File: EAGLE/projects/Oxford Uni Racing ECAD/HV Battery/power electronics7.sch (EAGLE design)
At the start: 57 parts, among them IC1 4043D, IC2 SE555D, IC6 4011D, K1 T9AS1D12-48=T9A, K2 T9AS5D12-12=T9A, K3 T9AS1D12-48=T9A, K4 T9AS1D12-48=T9A, K5 T9AS1D12-48=T9A, Q1 BSS138, Q2 BSS138, Q3 BSS138

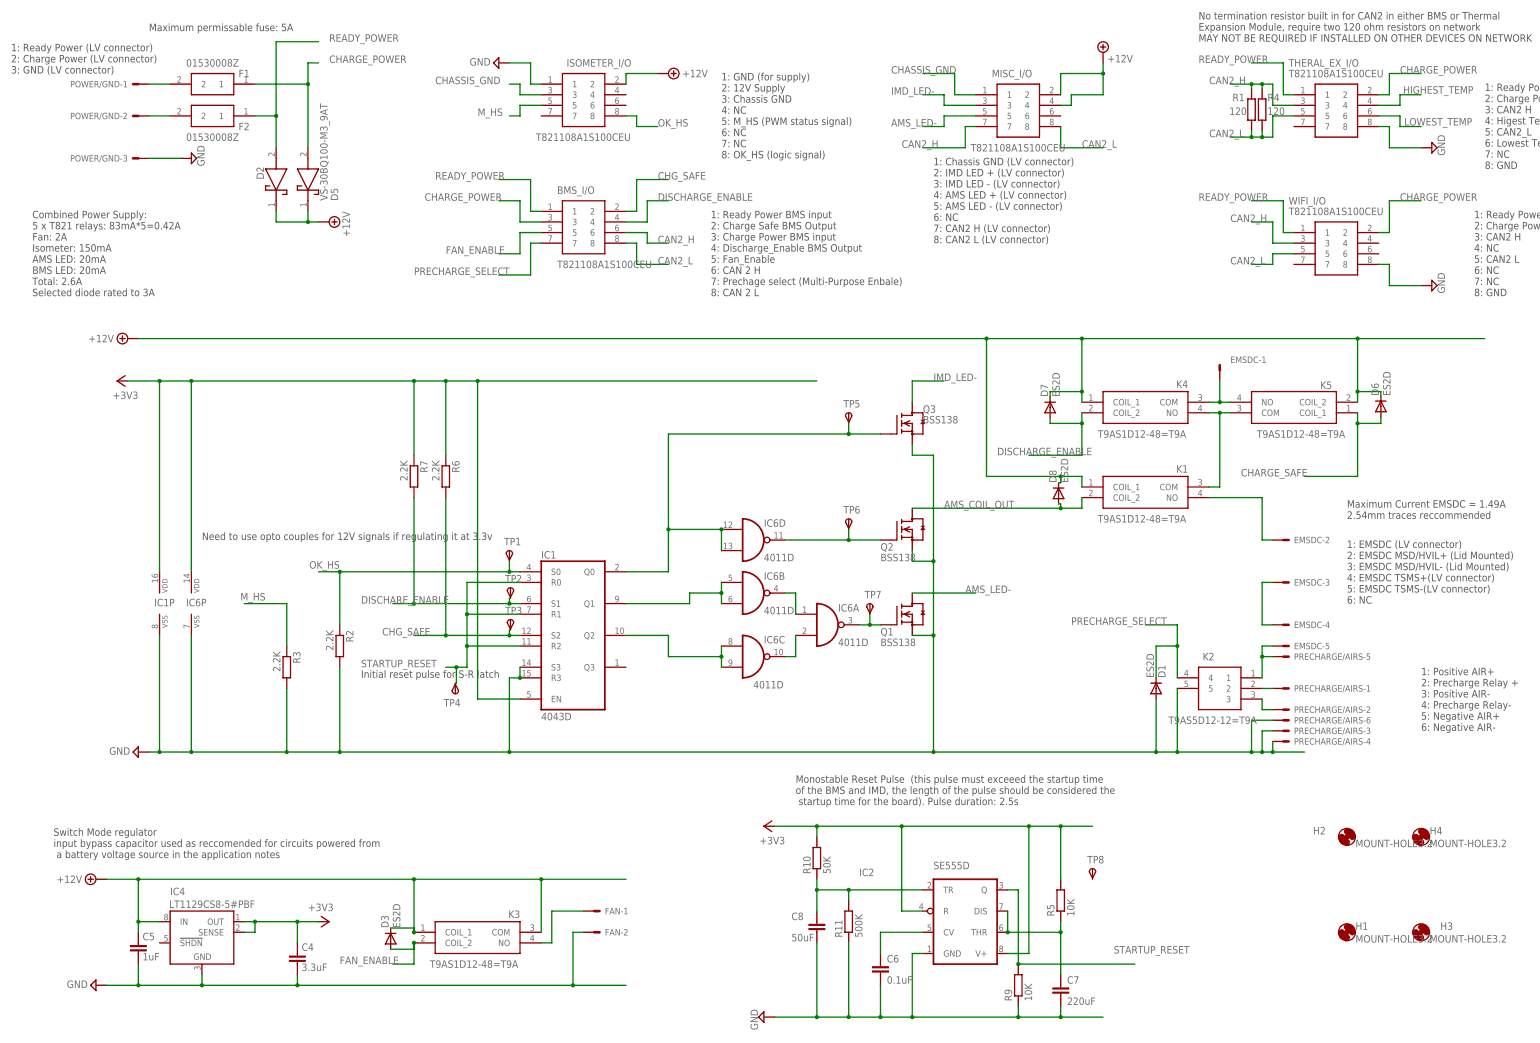
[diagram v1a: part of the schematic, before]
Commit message: Updated to include discharge/dischare enable bug, amended 555 passive compoenent values to match values in deptartment stores
Signed-off-by: Jack Bruford <jack.bruford41@gmail.com>
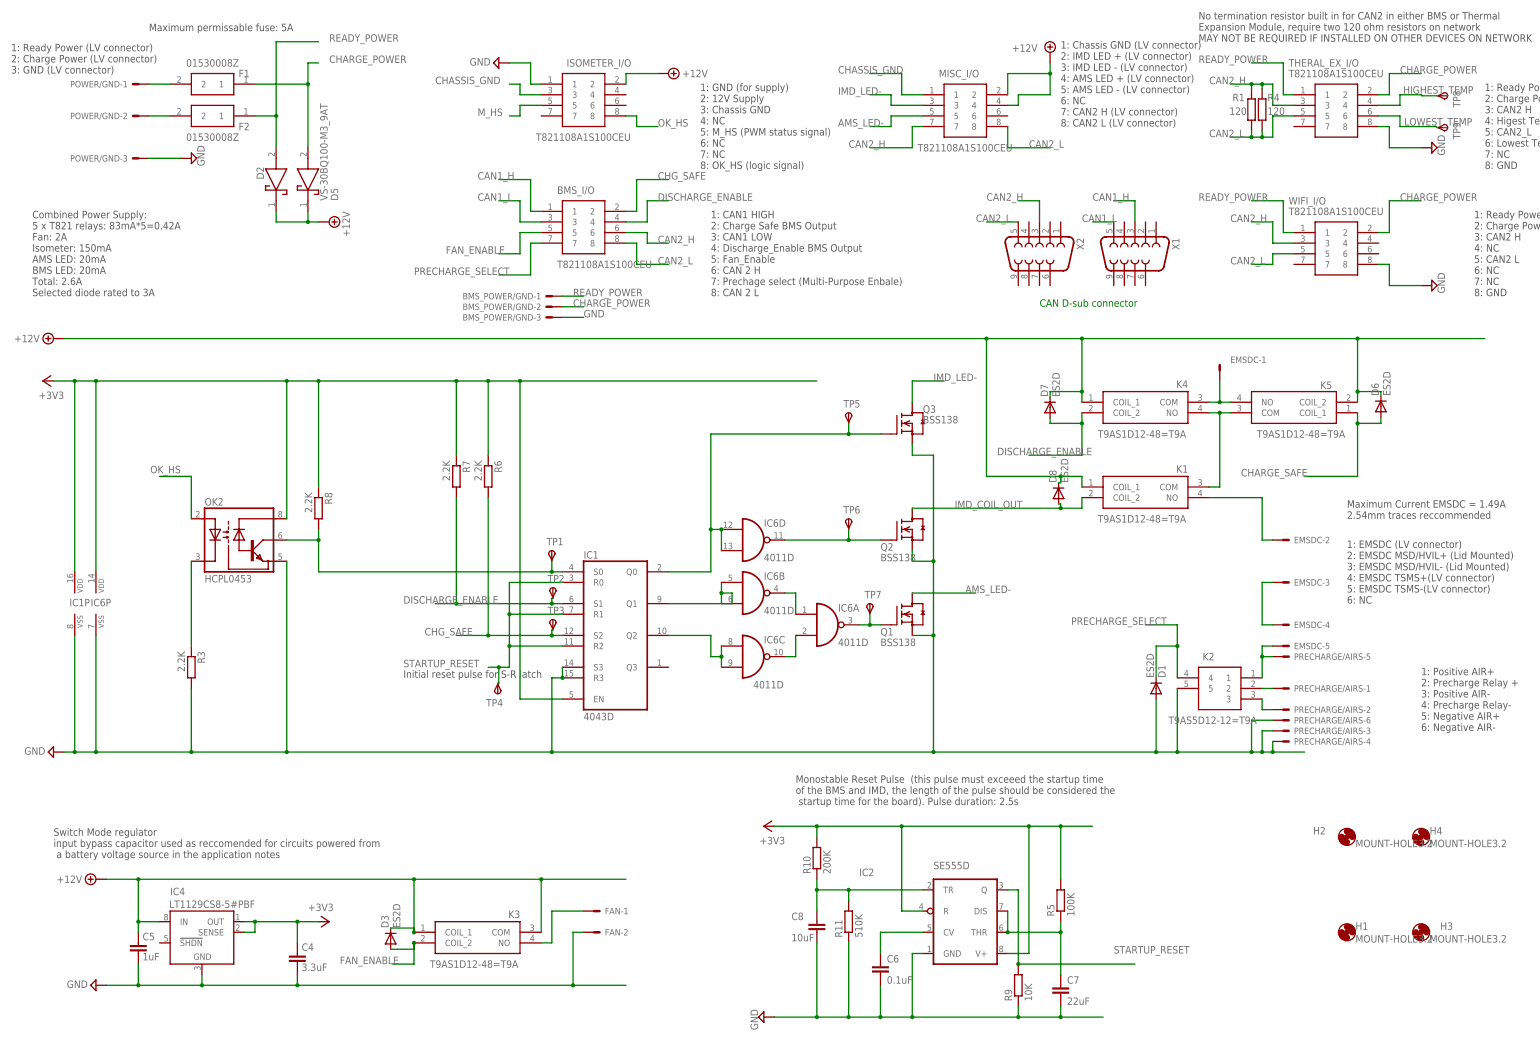
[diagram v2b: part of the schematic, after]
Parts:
- removed R2: 2.2K, rcl:R-EU_R1206
- added BMS_POWER/GND: (no value), con-molex:KK-156-3
- added OK2: HCPL0453, optocoupler:HCPL0453
- added R8: 2.2K, rcl:R-EU_R1206
- added TP9: TPSTP11R, testpad:TPSTP11R
- added X1, X2: (no value), con-subd:F09V
- C7: value 220uF -> 22uF
- C8: value 50uF -> 10uF
- R10: value 50K -> 200K
- R11: value 500K -> 510K
- R5: value 10K -> 100K
- TP8: value TPSTP17R -> TPSTP11R; device testpad:TPSTP17R -> testpad:TPSTP11R
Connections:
- net AMS_COIL_OUT renamed IMD_COIL_OUT
- removed net DISCHARE_ENABLE: IC1A.S1, R7.2, TP2.PP
- new net CAN1_H: BMS_I/O.1, X1.3
- new net CAN1_L: BMS_I/O.3, X1.5
- new net N$5: IC1A.S0, OK2.VO, R8.2, TP1.PP
- new net N$7: OK2.C, R3.1
- net +3V3: now also OK2.VCC, R8.1
- net CAN2_H: now also X2.3
- net CAN2_L: now also X2.5
- net CHARGE_POWER: now also BMS_POWER/GND-2.S; no longer BMS_I/O.3
- net DISCHARGE_ENABLE: now also IC1A.S1, R7.2, TP2.PP
- net GND: now also BMS_POWER/GND-3.S, OK2.GND; no longer R2.2
- net HIGHEST_TEMP: now also TP8.PP
- net LOWEST_TEMP: now also TP9.PP
- net M_HS: no longer R3.1
- net OK_HS: now also OK2.A; no longer IC1A.S0, R2.1, TP1.PP
- net READY_POWER: now also BMS_POWER/GND-1.S; no longer BMS_I/O.1
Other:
- note added: "1: CAN1 HIGH 2: Charge Safe BMS Output 3: CAN1 LOW 4: Discharge_Enable BMS Output 5: Fan_Enable 6: CAN 2 H 7: Prechage select (Multi-Purpose Enbale) 8: CAN 2 L"
- note added: "CAN D-sub connector"
- note removed: "1: Ready Power BMS input 2: Charge Safe BMS Output 3: Charge Power BMS input 4: Discharge_Enable BMS Output 5: Fan_Enable 6: CAN 2 H 7: Prechage select (Multi-Purpose Enbale) 8: CAN 2 L"
- note removed: "Need to use opto couples for 12V signals if regulating it at 3.3v"
- moved on the sheet: IC1, IC1P, IC6P, MISC_I/O, R3, R6, R7, TP1, TP2, TP3, TP4, TP8
